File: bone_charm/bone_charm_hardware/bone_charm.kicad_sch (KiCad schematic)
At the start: 13 parts, among them J1 Conn_ICSP, U1 ATmega328-A, U2 MCP4725xxx-xCH, Y1 Crystal

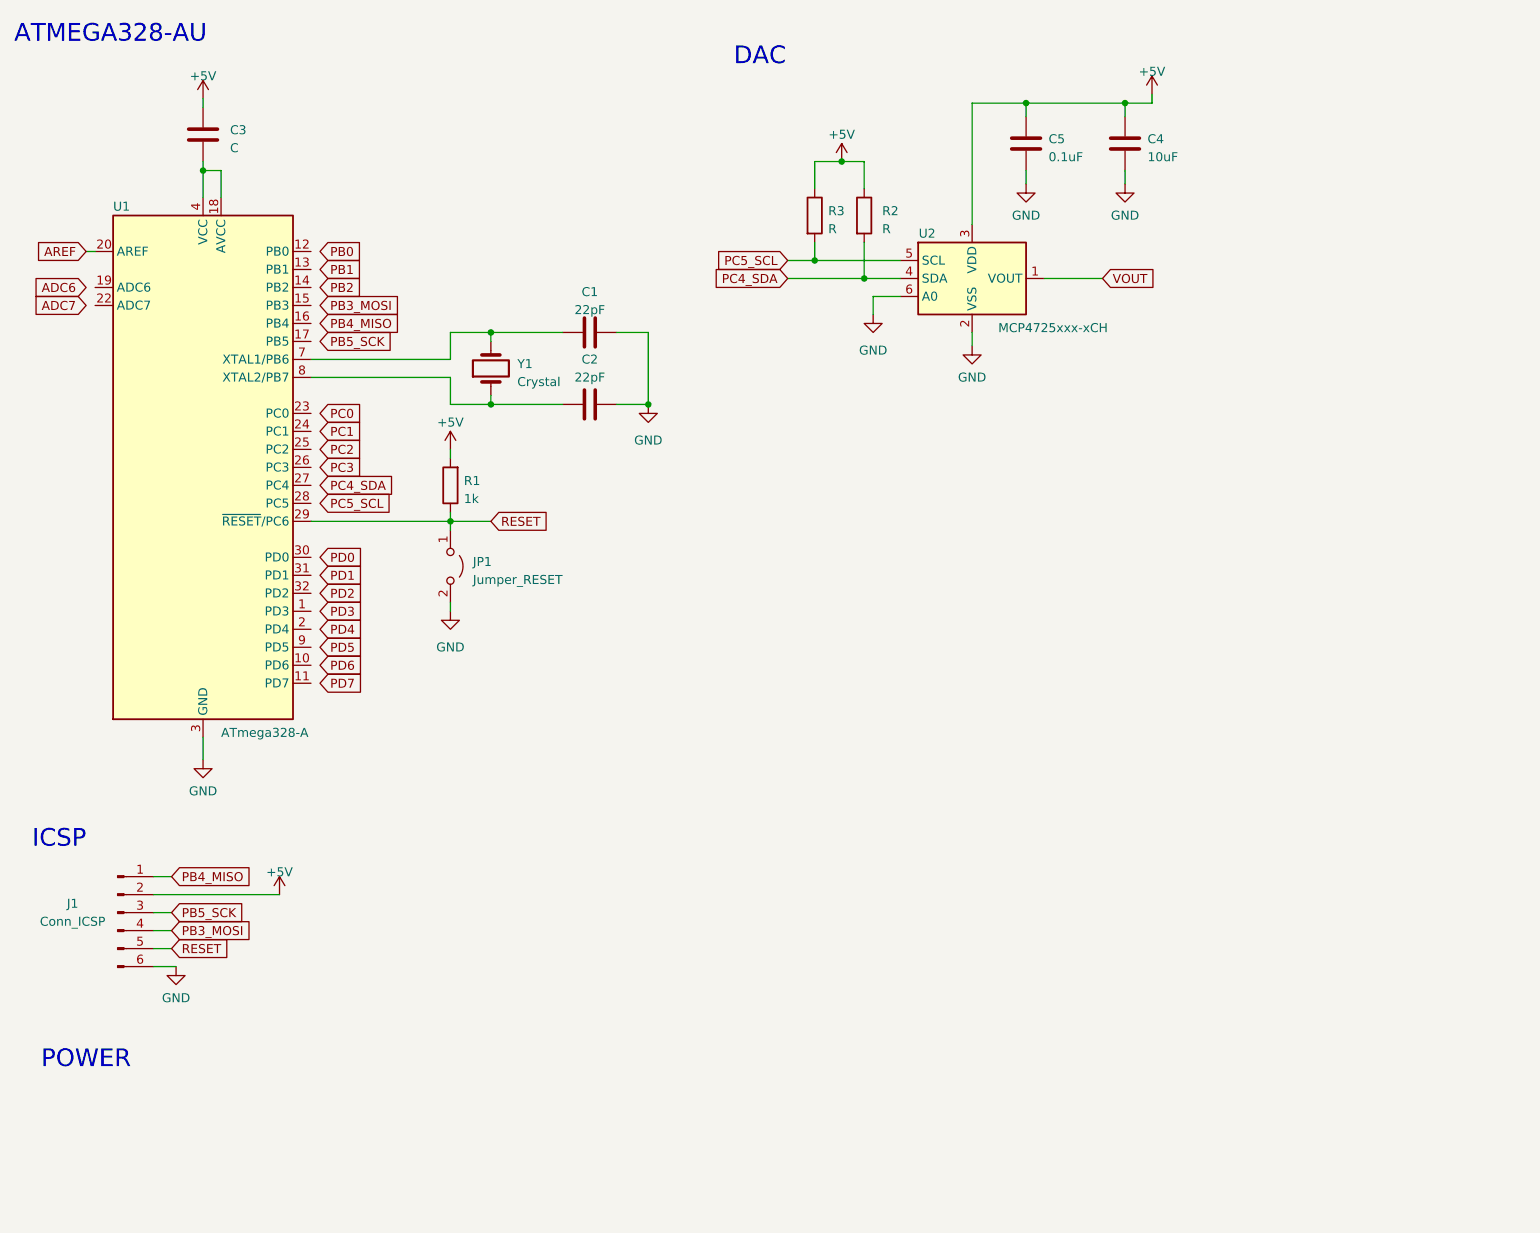
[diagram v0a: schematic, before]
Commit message: IO page added
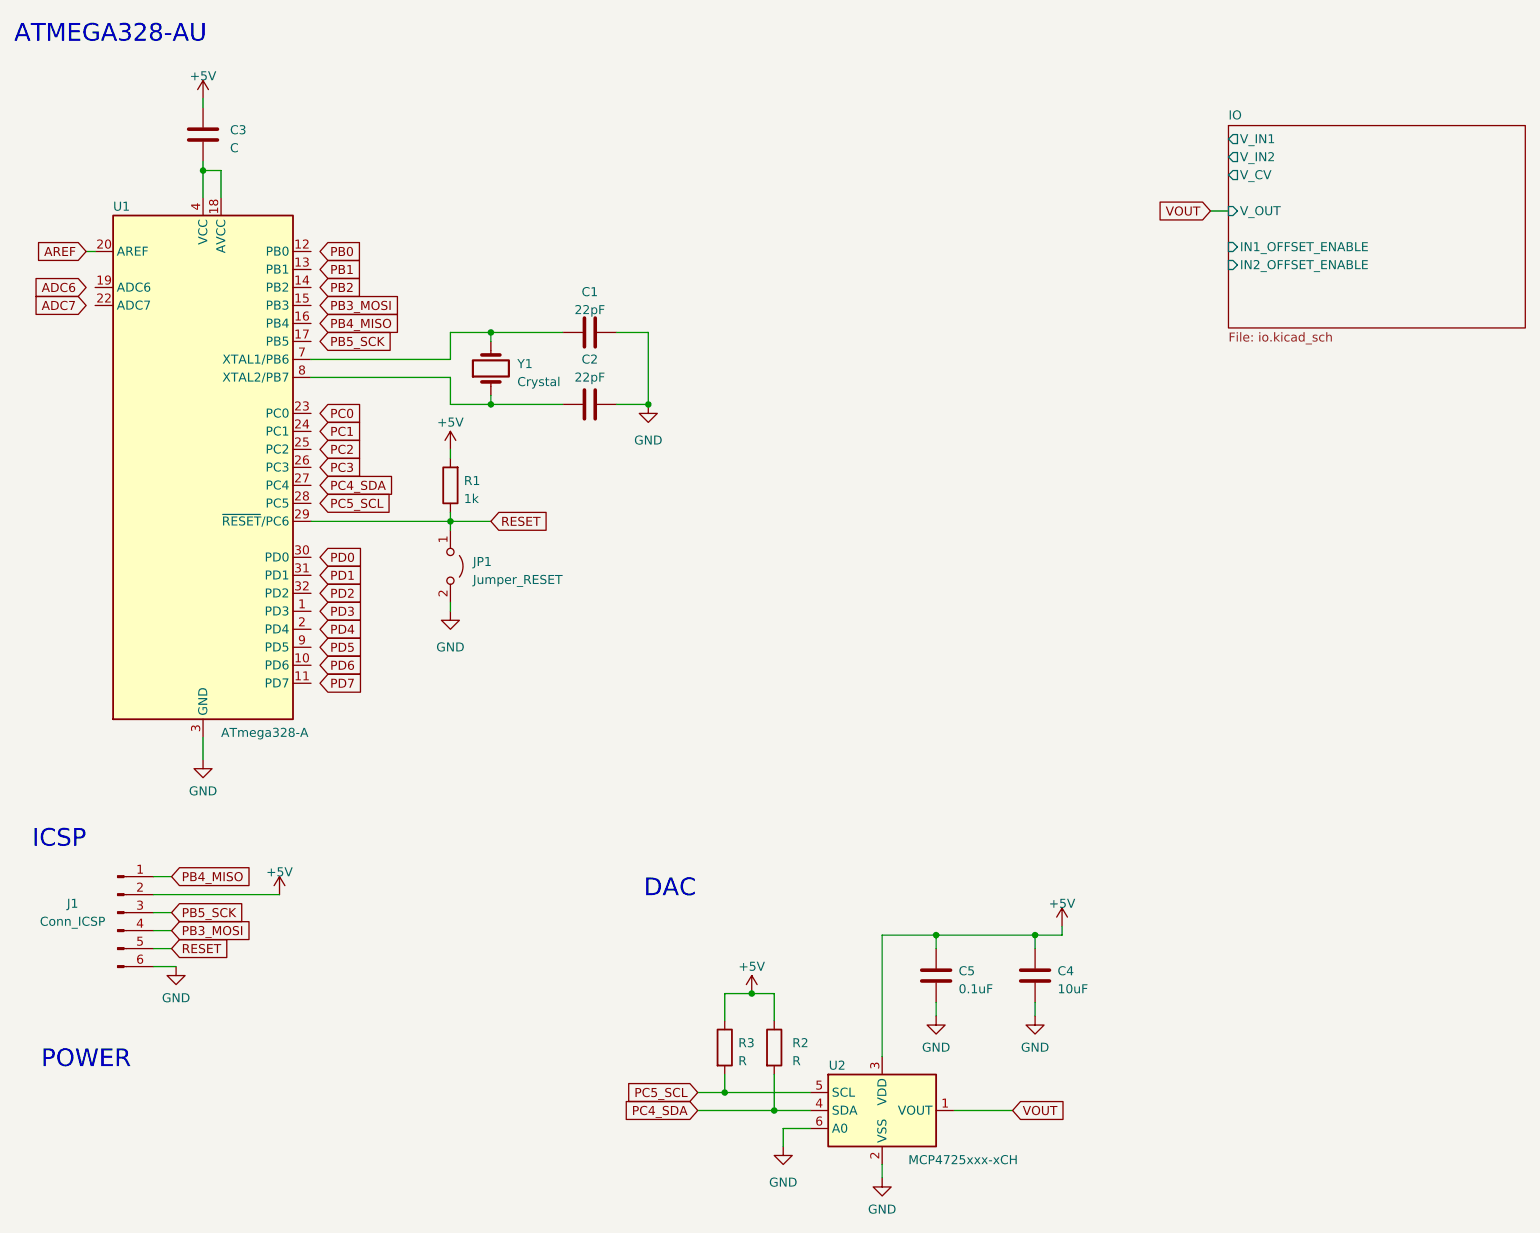
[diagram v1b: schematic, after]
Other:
- added sheet IO (io.kicad_sch)
- moved on the sheet: C4, C5, R2, R3, U2
